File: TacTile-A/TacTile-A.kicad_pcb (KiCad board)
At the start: 2 copper layers, 60 x 60 mm, 100 parts, among them J1 Conn_01x01, J2 Conn_01x01, J3 Conn_01x01, J4 Conn_01x01, U1 MCP14A0304xMNY, U10 MCP14A0304xMNY, U11 MCP14A0304xMNY, U12 MCP14A0304xMNY, U13 MCP14A0304xMNY, U14 MCP14A0304xMNY, U15 MCP14A0304xMNY, U16 MCP14A0304xMNY, U2 MCP14A0304xMNY, U3 MCP14A0304xMNY, U4 MCP14A0304xMNY, U5 MCP14A0304xMNY, U6 MCP14A0304xMNY, U7 MCP14A0304xMNY, U8 MCP14A0304xMNY, U9 MCP14A0304xMNY

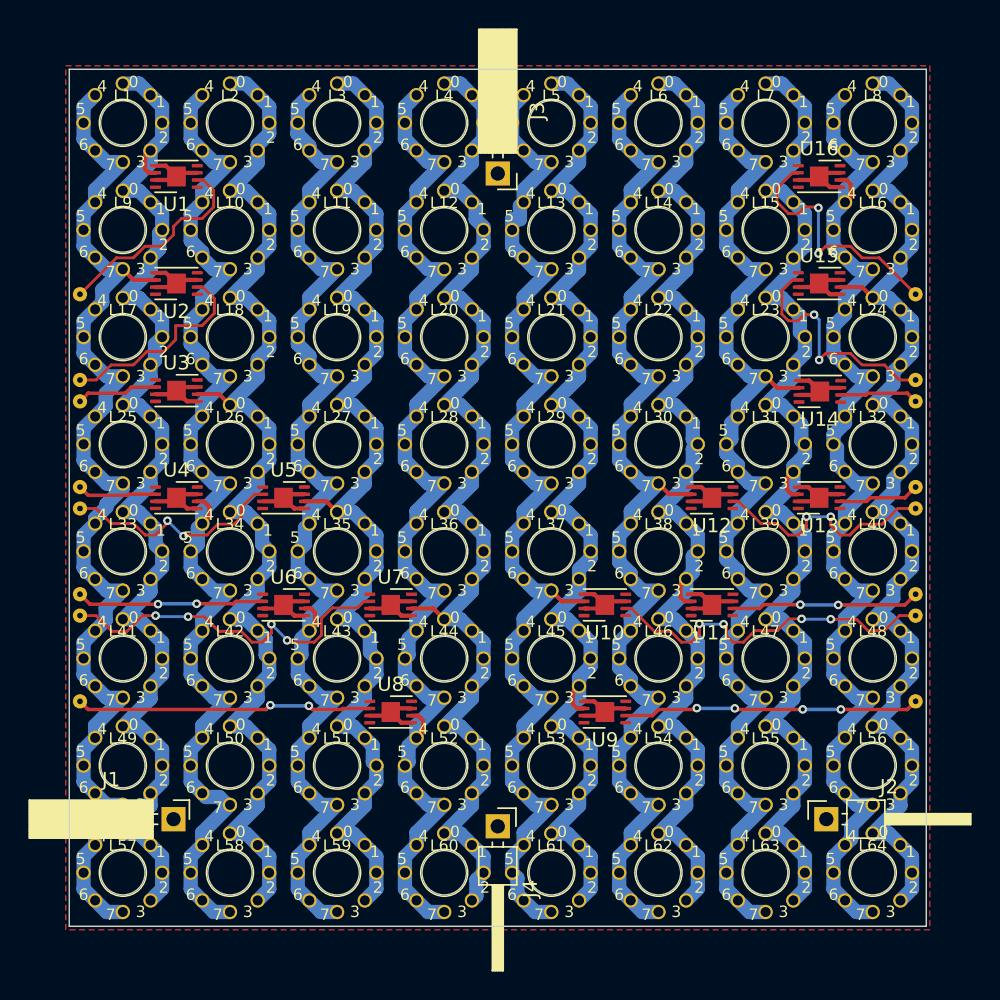
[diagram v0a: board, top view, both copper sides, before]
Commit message: Redid A board with MOSFETs sinking current
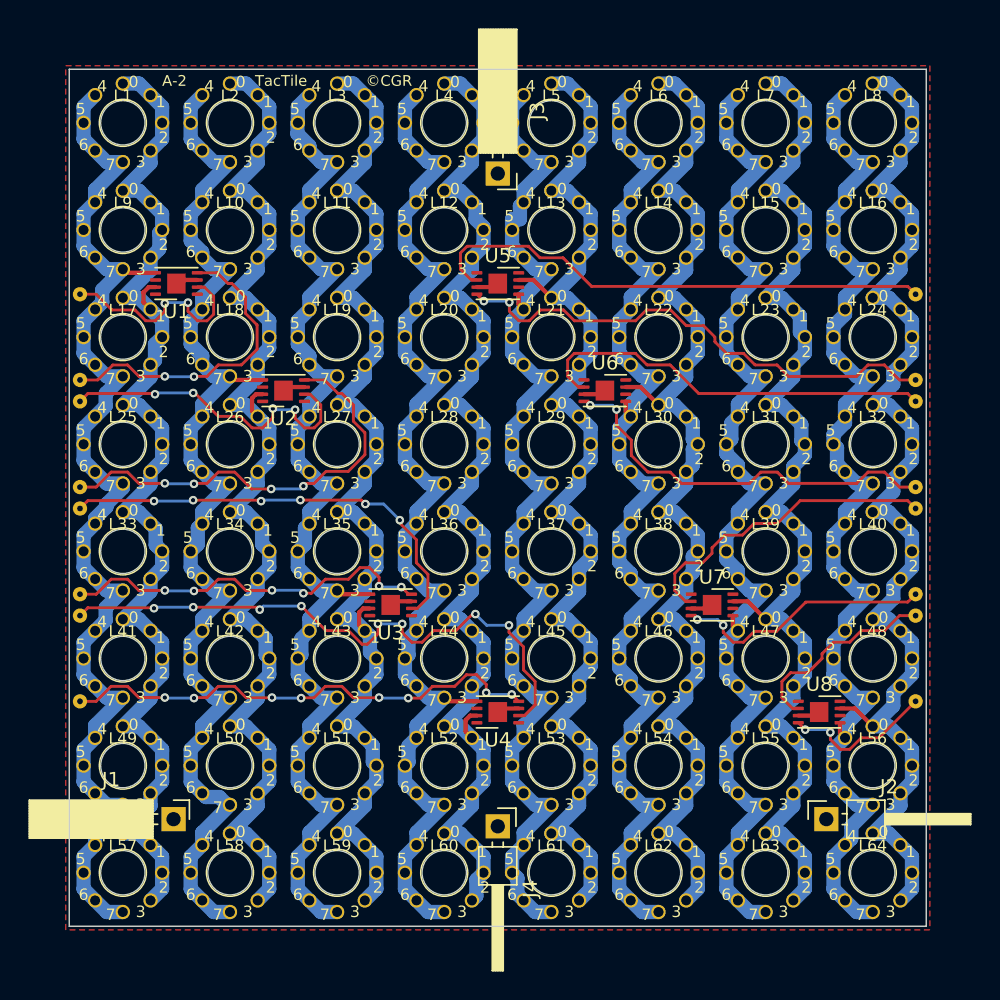
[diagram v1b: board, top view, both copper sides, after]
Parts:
- removed U13, U14, U15, U16: MCP14A0304xMNY, Package_DFN_QFN:WDFN-8-1EP_3x2mm_P0.5mm_EP1.3x1.4mm
- removed the U5 at (40.0, 55.0)
- removed the U6 at (40.0, 62.5)
- removed the U7 at (47.5, 62.5)
- removed the U8 at (47.5, 70.0)
- U1, U2, U3, U4: value MCP14A0304xMNY -> MCP14A0303xMNY
- U5: renamed from U9; value MCP14A0304xMNY -> MCP14A0303xMNY
- U6: renamed from U10; value MCP14A0304xMNY -> MCP14A0303xMNY
- U7: renamed from U11; value MCP14A0304xMNY -> MCP14A0303xMNY
- U8: renamed from U12; value MCP14A0304xMNY -> MCP14A0303xMNY
- moved U5 30.9 mm to (55.0, 40.0), turned to 0 degrees
- moved JMP16 28.5 mm to (84.2, 69.2), turned to 180 degrees
- moved JMP9 28.5 mm to (84.2, 40.8), turned to 180 degrees
- moved U4 27.0 mm to (55.0, 70.0), turned to 180 degrees
- moved U3 21.2 mm to (47.5, 62.5), turned to 180 degrees
- moved U8 16.8 mm to (77.5, 70.0), turned to 0 degrees
- moved JMP10 16.5 mm to (84.2, 46.8), turned to 180 degrees
- moved JMP15 16.5 mm to (84.2, 63.2), turned to 180 degrees
- moved U6 15.0 mm to (62.5, 47.5), turned to 0 degrees
- moved JMP11 13.5 mm to (84.2, 48.2), turned to 180 degrees
- moved JMP14 13.5 mm to (84.2, 61.8), turned to 180 degrees
- moved U2 10.6 mm to (40.0, 47.5)
- moved U1 7.50 mm to (32.5, 40.0)
- moved JMP12 1.50 mm to (84.2, 54.2), turned to 180 degrees
- moved JMP13 1.50 mm to (84.2, 55.8), turned to 180 degrees
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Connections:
- L1 pad 1: /GND1 -> /GND0
- L1 pad 2: /GND1 -> /GND0
- L1 pad 3: /GND1 -> /GND0
- L1 pad 4: /GND1 -> /GND0
- L1 pad 5: /GND2 -> /GND1
- L1 pad 6: /GND2 -> /GND1
- L1 pad 7: /GND2 -> /GND1
- L1 pad 8: /GND2 -> /GND1
- L10 pad 1: /GND3 -> /GND2
- L10 pad 2: /GND3 -> /GND2
- L10 pad 3: /GND3 -> /GND2
- L10 pad 4: /GND3 -> /GND2
- L10 pad 5: /GND4 -> /GND3
- L10 pad 6: /GND4 -> /GND3
- L10 pad 7: /GND4 -> /GND3
- L10 pad 8: /GND4 -> /GND3
- L11 pad 1: /GND5 -> /GND4
- L11 pad 2: /GND5 -> /GND4
- L11 pad 3: /GND5 -> /GND4
- L11 pad 4: /GND5 -> /GND4
- L11 pad 5: /GND6 -> /GND5
- L11 pad 6: /GND6 -> /GND5
- L11 pad 7: /GND6 -> /GND5
- L11 pad 8: /GND6 -> /GND5
- L12 pad 1: /GND7 -> /GND6
- L12 pad 2: /GND7 -> /GND6
- L12 pad 3: /GND7 -> /GND6
- L12 pad 4: /GND7 -> /GND6
- L12 pad 5: /GND8 -> /GND7
- L12 pad 6: /GND8 -> /GND7
- L12 pad 7: /GND8 -> /GND7
- L12 pad 8: /GND8 -> /GND7
- L13 pad 1: /GND9 -> /GND8
- L13 pad 2: /GND9 -> /GND8
- L13 pad 3: /GND9 -> /GND8
- L13 pad 4: /GND9 -> /GND8
- L13 pad 5: /GND10 -> /GND9
- L13 pad 6: /GND10 -> /GND9
- L13 pad 7: /GND10 -> /GND9
- L13 pad 8: /GND10 -> /GND9
- L14 pad 1: /GND11 -> /GND10
- L14 pad 2: /GND11 -> /GND10
- L14 pad 3: /GND11 -> /GND10
- L14 pad 4: /GND11 -> /GND10
- L14 pad 5: /GND12 -> /GND11
- L14 pad 6: /GND12 -> /GND11
- L14 pad 7: /GND12 -> /GND11
- L14 pad 8: /GND12 -> /GND11
- L15 pad 1: /GND13 -> /GND12
- L15 pad 2: /GND13 -> /GND12
- L15 pad 3: /GND13 -> /GND12
- L15 pad 4: /GND13 -> /GND12
- L15 pad 5: /GND14 -> /GND13
- L15 pad 6: /GND14 -> /GND13
- L15 pad 7: /GND14 -> /GND13
- L15 pad 8: /GND14 -> /GND13
- L16 pad 1: /GND15 -> /GND14
- L16 pad 2: /GND15 -> /GND14
- L16 pad 3: /GND15 -> /GND14
- L16 pad 4: /GND15 -> /GND14
- L16 pad 5: /GND16 -> /GND15
- L16 pad 6: /GND16 -> /GND15
- L16 pad 7: /GND16 -> /GND15
- L16 pad 8: /GND16 -> /GND15
- L17 pad 1: /GND1 -> /GND0
- L17 pad 2: /GND1 -> /GND0
- L17 pad 3: /GND1 -> /GND0
- L17 pad 4: /GND1 -> /GND0
- L17 pad 5: /GND2 -> /GND1
- L17 pad 6: /GND2 -> /GND1
- L17 pad 7: /GND2 -> /GND1
- L17 pad 8: /GND2 -> /GND1
- L18 pad 1: /GND3 -> /GND2
- L18 pad 2: /GND3 -> /GND2
- L18 pad 3: /GND3 -> /GND2
- L18 pad 4: /GND3 -> /GND2
- L18 pad 5: /GND4 -> /GND3
- L18 pad 6: /GND4 -> /GND3
- L18 pad 7: /GND4 -> /GND3
- L18 pad 8: /GND4 -> /GND3
- L19 pad 1: /GND5 -> /GND4
- L19 pad 2: /GND5 -> /GND4
- L19 pad 3: /GND5 -> /GND4
- L19 pad 4: /GND5 -> /GND4
- L19 pad 5: /GND6 -> /GND5
- L19 pad 6: /GND6 -> /GND5
- L19 pad 7: /GND6 -> /GND5
- L19 pad 8: /GND6 -> /GND5
- L2 pad 1: /GND3 -> /GND2
- L2 pad 2: /GND3 -> /GND2
- L2 pad 3: /GND3 -> /GND2
- L2 pad 4: /GND3 -> /GND2
- L2 pad 5: /GND4 -> /GND3
- L2 pad 6: /GND4 -> /GND3
- L2 pad 7: /GND4 -> /GND3
- L2 pad 8: /GND4 -> /GND3
- L20 pad 1: /GND7 -> /GND6
- L20 pad 2: /GND7 -> /GND6
- L20 pad 3: /GND7 -> /GND6
- L20 pad 4: /GND7 -> /GND6
- L20 pad 5: /GND8 -> /GND7
- L20 pad 6: /GND8 -> /GND7
- L20 pad 7: /GND8 -> /GND7
- L20 pad 8: /GND8 -> /GND7
- L21 pad 1: /GND9 -> /GND8
- L21 pad 2: /GND9 -> /GND8
- L21 pad 3: /GND9 -> /GND8
- L21 pad 4: /GND9 -> /GND8
- L21 pad 5: /GND10 -> /GND9
- L21 pad 6: /GND10 -> /GND9
- L21 pad 7: /GND10 -> /GND9
- L21 pad 8: /GND10 -> /GND9
- L22 pad 1: /GND11 -> /GND10
- L22 pad 2: /GND11 -> /GND10
- L22 pad 3: /GND11 -> /GND10
- L22 pad 4: /GND11 -> /GND10
- L22 pad 5: /GND12 -> /GND11
- L22 pad 6: /GND12 -> /GND11
- L22 pad 7: /GND12 -> /GND11
- L22 pad 8: /GND12 -> /GND11
- L23 pad 1: /GND13 -> /GND12
- L23 pad 2: /GND13 -> /GND12
- L23 pad 3: /GND13 -> /GND12
- L23 pad 4: /GND13 -> /GND12
- L23 pad 5: /GND14 -> /GND13
- L23 pad 6: /GND14 -> /GND13
- L23 pad 7: /GND14 -> /GND13
- L23 pad 8: /GND14 -> /GND13
- L24 pad 1: /GND15 -> /GND14
- L24 pad 2: /GND15 -> /GND14
- L24 pad 3: /GND15 -> /GND14
- L24 pad 4: /GND15 -> /GND14
- L24 pad 5: /GND16 -> /GND15
- L24 pad 6: /GND16 -> /GND15
- L24 pad 7: /GND16 -> /GND15
- L24 pad 8: /GND16 -> /GND15
- L25 pad 1: /GND1 -> /GND0
- L25 pad 2: /GND1 -> /GND0
- L25 pad 3: /GND1 -> /GND0
- L25 pad 4: /GND1 -> /GND0
- L25 pad 5: /GND2 -> /GND1
- L25 pad 6: /GND2 -> /GND1
- L25 pad 7: /GND2 -> /GND1
- L25 pad 8: /GND2 -> /GND1
- L26 pad 1: /GND3 -> /GND2
- L26 pad 2: /GND3 -> /GND2
- L26 pad 3: /GND3 -> /GND2
- L26 pad 4: /GND3 -> /GND2
- L26 pad 5: /GND4 -> /GND3
- L26 pad 6: /GND4 -> /GND3
- L26 pad 7: /GND4 -> /GND3
- L26 pad 8: /GND4 -> /GND3
- L27 pad 1: /GND5 -> /GND4
- L27 pad 2: /GND5 -> /GND4
- L27 pad 3: /GND5 -> /GND4
- L27 pad 4: /GND5 -> /GND4
- L27 pad 5: /GND6 -> /GND5
- L27 pad 6: /GND6 -> /GND5
- L27 pad 7: /GND6 -> /GND5
- L27 pad 8: /GND6 -> /GND5
- L28 pad 1: /GND7 -> /GND6
- L28 pad 2: /GND7 -> /GND6
- L28 pad 3: /GND7 -> /GND6
- L28 pad 4: /GND7 -> /GND6
- L28 pad 5: /GND8 -> /GND7
- L28 pad 6: /GND8 -> /GND7
- L28 pad 7: /GND8 -> /GND7
- L28 pad 8: /GND8 -> /GND7
- L29 pad 1: /GND9 -> /GND8
- L29 pad 2: /GND9 -> /GND8
- L29 pad 3: /GND9 -> /GND8
- L29 pad 4: /GND9 -> /GND8
- L29 pad 5: /GND10 -> /GND9
- L29 pad 6: /GND10 -> /GND9
- L29 pad 7: /GND10 -> /GND9
- L29 pad 8: /GND10 -> /GND9
- L3 pad 1: /GND5 -> /GND4
- L3 pad 2: /GND5 -> /GND4
- L3 pad 3: /GND5 -> /GND4
- L3 pad 4: /GND5 -> /GND4
- L3 pad 5: /GND6 -> /GND5
- L3 pad 6: /GND6 -> /GND5
- L3 pad 7: /GND6 -> /GND5
- L3 pad 8: /GND6 -> /GND5
- L30 pad 1: /GND11 -> /GND10
- L30 pad 2: /GND11 -> /GND10
- L30 pad 3: /GND11 -> /GND10
- L30 pad 4: /GND11 -> /GND10
- L30 pad 5: /GND12 -> /GND11
- L30 pad 6: /GND12 -> /GND11
- L30 pad 7: /GND12 -> /GND11
- L30 pad 8: /GND12 -> /GND11
- L31 pad 1: /GND13 -> /GND12
- L31 pad 2: /GND13 -> /GND12
- L31 pad 3: /GND13 -> /GND12
- L31 pad 4: /GND13 -> /GND12
- L31 pad 5: /GND14 -> /GND13
- L31 pad 6: /GND14 -> /GND13
- L31 pad 7: /GND14 -> /GND13
- L31 pad 8: /GND14 -> /GND13
- L32 pad 1: /GND15 -> /GND14
- L32 pad 2: /GND15 -> /GND14
- L32 pad 3: /GND15 -> /GND14
- L32 pad 4: /GND15 -> /GND14
- L32 pad 5: /GND16 -> /GND15
- L32 pad 6: /GND16 -> /GND15
- L32 pad 7: /GND16 -> /GND15
- L32 pad 8: /GND16 -> /GND15
- L33 pad 1: /GND1 -> /GND0
- L33 pad 2: /GND1 -> /GND0
- L33 pad 3: /GND1 -> /GND0
- L33 pad 4: /GND1 -> /GND0
- L33 pad 5: /GND2 -> /GND1
- L33 pad 6: /GND2 -> /GND1
- L33 pad 7: /GND2 -> /GND1
- L33 pad 8: /GND2 -> /GND1
- L34 pad 1: /GND3 -> /GND2
- L34 pad 2: /GND3 -> /GND2
- L34 pad 3: /GND3 -> /GND2
- L34 pad 4: /GND3 -> /GND2
- L34 pad 5: /GND4 -> /GND3
- L34 pad 6: /GND4 -> /GND3
- L34 pad 7: /GND4 -> /GND3
- L34 pad 8: /GND4 -> /GND3
- L35 pad 1: /GND5 -> /GND4
- L35 pad 2: /GND5 -> /GND4
- L35 pad 3: /GND5 -> /GND4
- L35 pad 4: /GND5 -> /GND4
- L35 pad 5: /GND6 -> /GND5
- L35 pad 6: /GND6 -> /GND5
- L35 pad 7: /GND6 -> /GND5
- L35 pad 8: /GND6 -> /GND5
- L36 pad 1: /GND7 -> /GND6
- L36 pad 2: /GND7 -> /GND6
- L36 pad 3: /GND7 -> /GND6
- L36 pad 4: /GND7 -> /GND6
- L36 pad 5: /GND8 -> /GND7
- L36 pad 6: /GND8 -> /GND7
- L36 pad 7: /GND8 -> /GND7
- L36 pad 8: /GND8 -> /GND7
- L37 pad 1: /GND9 -> /GND8
- L37 pad 2: /GND9 -> /GND8
- L37 pad 3: /GND9 -> /GND8
- L37 pad 4: /GND9 -> /GND8
- L37 pad 5: /GND10 -> /GND9
- L37 pad 6: /GND10 -> /GND9
- L37 pad 7: /GND10 -> /GND9
- L37 pad 8: /GND10 -> /GND9
- L38 pad 1: /GND11 -> /GND10
- L38 pad 2: /GND11 -> /GND10
- L38 pad 3: /GND11 -> /GND10
- L38 pad 4: /GND11 -> /GND10
- L38 pad 5: /GND12 -> /GND11
- L38 pad 6: /GND12 -> /GND11
- L38 pad 7: /GND12 -> /GND11
- L38 pad 8: /GND12 -> /GND11
- L39 pad 1: /GND13 -> /GND12
- L39 pad 2: /GND13 -> /GND12
- L39 pad 3: /GND13 -> /GND12
- L39 pad 4: /GND13 -> /GND12
- L39 pad 5: /GND14 -> /GND13
- L39 pad 6: /GND14 -> /GND13
- L39 pad 7: /GND14 -> /GND13
- L39 pad 8: /GND14 -> /GND13
- L4 pad 1: /GND7 -> /GND6
- L4 pad 2: /GND7 -> /GND6
- L4 pad 3: /GND7 -> /GND6
- L4 pad 4: /GND7 -> /GND6
- L4 pad 5: /GND8 -> /GND7
- L4 pad 6: /GND8 -> /GND7
- L4 pad 7: /GND8 -> /GND7
- L4 pad 8: /GND8 -> /GND7
- L40 pad 1: /GND15 -> /GND14
- L40 pad 2: /GND15 -> /GND14
- L40 pad 3: /GND15 -> /GND14
- L40 pad 4: /GND15 -> /GND14
- L40 pad 5: /GND16 -> /GND15
- L40 pad 6: /GND16 -> /GND15
- L40 pad 7: /GND16 -> /GND15
- L40 pad 8: /GND16 -> /GND15
- L41 pad 1: /GND1 -> /GND0
- L41 pad 2: /GND1 -> /GND0
- L41 pad 3: /GND1 -> /GND0
- L41 pad 4: /GND1 -> /GND0
- L41 pad 5: /GND2 -> /GND1
- L41 pad 6: /GND2 -> /GND1
- L41 pad 7: /GND2 -> /GND1
- L41 pad 8: /GND2 -> /GND1
- L42 pad 1: /GND3 -> /GND2
- L42 pad 2: /GND3 -> /GND2
- L42 pad 3: /GND3 -> /GND2
- L42 pad 4: /GND3 -> /GND2
- L42 pad 5: /GND4 -> /GND3
- L42 pad 6: /GND4 -> /GND3
- L42 pad 7: /GND4 -> /GND3
- L42 pad 8: /GND4 -> /GND3
- L43 pad 1: /GND5 -> /GND4
- L43 pad 2: /GND5 -> /GND4
- L43 pad 3: /GND5 -> /GND4
- L43 pad 4: /GND5 -> /GND4
- L43 pad 5: /GND6 -> /GND5
- L43 pad 6: /GND6 -> /GND5
- L43 pad 7: /GND6 -> /GND5
- L43 pad 8: /GND6 -> /GND5
- L44 pad 1: /GND7 -> /GND6
- L44 pad 2: /GND7 -> /GND6
- L44 pad 3: /GND7 -> /GND6
- L44 pad 4: /GND7 -> /GND6
- L44 pad 5: /GND8 -> /GND7
- L44 pad 6: /GND8 -> /GND7
- L44 pad 7: /GND8 -> /GND7
- L44 pad 8: /GND8 -> /GND7
- L45 pad 1: /GND9 -> /GND8
- L45 pad 2: /GND9 -> /GND8
- L45 pad 3: /GND9 -> /GND8
- L45 pad 4: /GND9 -> /GND8
- L45 pad 5: /GND10 -> /GND9
- L45 pad 6: /GND10 -> /GND9
- L45 pad 7: /GND10 -> /GND9
- L45 pad 8: /GND10 -> /GND9
- L46 pad 1: /GND11 -> /GND10
- L46 pad 2: /GND11 -> /GND10
- L46 pad 3: /GND11 -> /GND10
- L46 pad 4: /GND11 -> /GND10
- L46 pad 5: /GND12 -> /GND11
- L46 pad 6: /GND12 -> /GND11
- L46 pad 7: /GND12 -> /GND11
- L46 pad 8: /GND12 -> /GND11
- L47 pad 1: /GND13 -> /GND12
- L47 pad 2: /GND13 -> /GND12
- L47 pad 3: /GND13 -> /GND12
- L47 pad 4: /GND13 -> /GND12
- L47 pad 5: /GND14 -> /GND13
- L47 pad 6: /GND14 -> /GND13
- L47 pad 7: /GND14 -> /GND13
- L47 pad 8: /GND14 -> /GND13
- L48 pad 1: /GND15 -> /GND14
- L48 pad 2: /GND15 -> /GND14
- L48 pad 3: /GND15 -> /GND14
- L48 pad 4: /GND15 -> /GND14
- L48 pad 5: /GND16 -> /GND15
- L48 pad 6: /GND16 -> /GND15
- L48 pad 7: /GND16 -> /GND15
- L48 pad 8: /GND16 -> /GND15
- L49 pad 1: /GND1 -> /GND0
- L49 pad 2: /GND1 -> /GND0
- L49 pad 3: /GND1 -> /GND0
- L49 pad 4: /GND1 -> /GND0
- L49 pad 5: /GND2 -> /GND1
- L49 pad 6: /GND2 -> /GND1
- L49 pad 7: /GND2 -> /GND1
- L49 pad 8: /GND2 -> /GND1
- L5 pad 1: /GND9 -> /GND8
- L5 pad 2: /GND9 -> /GND8
- L5 pad 3: /GND9 -> /GND8
- L5 pad 4: /GND9 -> /GND8
- L5 pad 5: /GND10 -> /GND9
- L5 pad 6: /GND10 -> /GND9
- L5 pad 7: /GND10 -> /GND9
- L5 pad 8: /GND10 -> /GND9
- L50 pad 1: /GND3 -> /GND2
- L50 pad 2: /GND3 -> /GND2
- L50 pad 3: /GND3 -> /GND2
- L50 pad 4: /GND3 -> /GND2
- L50 pad 5: /GND4 -> /GND3
- L50 pad 6: /GND4 -> /GND3
- L50 pad 7: /GND4 -> /GND3
- L50 pad 8: /GND4 -> /GND3
- L51 pad 1: /GND5 -> /GND4
- L51 pad 2: /GND5 -> /GND4
- L51 pad 3: /GND5 -> /GND4
- L51 pad 4: /GND5 -> /GND4
- L51 pad 5: /GND6 -> /GND5
- L51 pad 6: /GND6 -> /GND5
- L51 pad 7: /GND6 -> /GND5
- L51 pad 8: /GND6 -> /GND5
- L52 pad 1: /GND7 -> /GND6
- L52 pad 2: /GND7 -> /GND6
- L52 pad 3: /GND7 -> /GND6
- L52 pad 4: /GND7 -> /GND6
- L52 pad 5: /GND8 -> /GND7
- L52 pad 6: /GND8 -> /GND7
- L52 pad 7: /GND8 -> /GND7
- L52 pad 8: /GND8 -> /GND7
- L53 pad 1: /GND9 -> /GND8
- L53 pad 2: /GND9 -> /GND8
- L53 pad 3: /GND9 -> /GND8
- L53 pad 4: /GND9 -> /GND8
- L53 pad 5: /GND10 -> /GND9
- L53 pad 6: /GND10 -> /GND9
- L53 pad 7: /GND10 -> /GND9
- L53 pad 8: /GND10 -> /GND9
- L54 pad 1: /GND11 -> /GND10
- L54 pad 2: /GND11 -> /GND10
- L54 pad 3: /GND11 -> /GND10
- L54 pad 4: /GND11 -> /GND10
- L54 pad 5: /GND12 -> /GND11
- L54 pad 6: /GND12 -> /GND11
- L54 pad 7: /GND12 -> /GND11
- L54 pad 8: /GND12 -> /GND11
- L55 pad 1: /GND13 -> /GND12
- L55 pad 2: /GND13 -> /GND12
- L55 pad 3: /GND13 -> /GND12
- L55 pad 4: /GND13 -> /GND12
- L55 pad 5: /GND14 -> /GND13
- L55 pad 6: /GND14 -> /GND13
- L55 pad 7: /GND14 -> /GND13
- L55 pad 8: /GND14 -> /GND13
- L56 pad 1: /GND15 -> /GND14
- L56 pad 2: /GND15 -> /GND14
- L56 pad 3: /GND15 -> /GND14
- L56 pad 4: /GND15 -> /GND14
- L56 pad 5: /GND16 -> /GND15
- L56 pad 6: /GND16 -> /GND15
- L56 pad 7: /GND16 -> /GND15
- L56 pad 8: /GND16 -> /GND15
- L57 pad 1: /GND1 -> /GND0
- L57 pad 2: /GND1 -> /GND0
- L57 pad 3: /GND1 -> /GND0
- L57 pad 4: /GND1 -> /GND0
- L57 pad 5: /GND2 -> /GND1
- L57 pad 6: /GND2 -> /GND1
- L57 pad 7: /GND2 -> /GND1
- L57 pad 8: /GND2 -> /GND1
- L58 pad 1: /GND3 -> /GND2
- L58 pad 2: /GND3 -> /GND2
- L58 pad 3: /GND3 -> /GND2
- L58 pad 4: /GND3 -> /GND2
- L58 pad 5: /GND4 -> /GND3
- L58 pad 6: /GND4 -> /GND3
- L58 pad 7: /GND4 -> /GND3
- L58 pad 8: /GND4 -> /GND3
- L59 pad 1: /GND5 -> /GND4
- L59 pad 2: /GND5 -> /GND4
- L59 pad 3: /GND5 -> /GND4
- L59 pad 4: /GND5 -> /GND4
- L59 pad 5: /GND6 -> /GND5
- L59 pad 6: /GND6 -> /GND5
- L59 pad 7: /GND6 -> /GND5
- L59 pad 8: /GND6 -> /GND5
- L6 pad 1: /GND11 -> /GND10
- L6 pad 2: /GND11 -> /GND10
- L6 pad 3: /GND11 -> /GND10
- L6 pad 4: /GND11 -> /GND10
- L6 pad 5: /GND12 -> /GND11
- L6 pad 6: /GND12 -> /GND11
- L6 pad 7: /GND12 -> /GND11
- L6 pad 8: /GND12 -> /GND11
- L60 pad 1: /GND7 -> /GND6
- L60 pad 2: /GND7 -> /GND6
- L60 pad 3: /GND7 -> /GND6
- L60 pad 4: /GND7 -> /GND6
- L60 pad 5: /GND8 -> /GND7
- L60 pad 6: /GND8 -> /GND7
- L60 pad 7: /GND8 -> /GND7
- L60 pad 8: /GND8 -> /GND7
- L61 pad 1: /GND9 -> /GND8
- L61 pad 2: /GND9 -> /GND8
- L61 pad 3: /GND9 -> /GND8
- L61 pad 4: /GND9 -> /GND8
- L61 pad 5: /GND10 -> /GND9
- L61 pad 6: /GND10 -> /GND9
- L61 pad 7: /GND10 -> /GND9
- L61 pad 8: /GND10 -> /GND9
- L62 pad 1: /GND11 -> /GND10
- L62 pad 2: /GND11 -> /GND10
- L62 pad 3: /GND11 -> /GND10
- L62 pad 4: /GND11 -> /GND10
- L62 pad 5: /GND12 -> /GND11
- L62 pad 6: /GND12 -> /GND11
- L62 pad 7: /GND12 -> /GND11
- L62 pad 8: /GND12 -> /GND11
- L63 pad 1: /GND13 -> /GND12
- L63 pad 2: /GND13 -> /GND12
- L63 pad 3: /GND13 -> /GND12
- L63 pad 4: /GND13 -> /GND12
- L63 pad 5: /GND14 -> /GND13
- L63 pad 6: /GND14 -> /GND13
- L63 pad 7: /GND14 -> /GND13
- L63 pad 8: /GND14 -> /GND13
- L64 pad 1: /GND15 -> /GND14
- L64 pad 2: /GND15 -> /GND14
- L64 pad 3: /GND15 -> /GND14
- L64 pad 4: /GND15 -> /GND14
- L64 pad 5: /GND16 -> /GND15
- L64 pad 6: /GND16 -> /GND15
- L64 pad 7: /GND16 -> /GND15
- L64 pad 8: /GND16 -> /GND15
- L7 pad 1: /GND13 -> /GND12
- L7 pad 2: /GND13 -> /GND12
- L7 pad 3: /GND13 -> /GND12
- L7 pad 4: /GND13 -> /GND12
- L7 pad 5: /GND14 -> /GND13
- L7 pad 6: /GND14 -> /GND13
- L7 pad 7: /GND14 -> /GND13
- L7 pad 8: /GND14 -> /GND13
- L8 pad 1: /GND15 -> /GND14
- L8 pad 2: /GND15 -> /GND14
- L8 pad 3: /GND15 -> /GND14
- L8 pad 4: /GND15 -> /GND14
- L8 pad 5: /GND16 -> /GND15
- L8 pad 6: /GND16 -> /GND15
- L8 pad 7: /GND16 -> /GND15
- L8 pad 8: /GND16 -> /GND15
- L9 pad 1: /GND1 -> /GND0
- L9 pad 2: /GND1 -> /GND0
- L9 pad 3: /GND1 -> /GND0
- L9 pad 4: /GND1 -> /GND0
- L9 pad 5: /GND2 -> /GND1
- L9 pad 6: /GND2 -> /GND1
- L9 pad 7: /GND2 -> /GND1
- L9 pad 8: /GND2 -> /GND1
- U1 pad 4: unconnected-(U1-INB-Pad4) -> /INP1
- U1 pad 5: /GND -> /GND1
- U1 pad 6: /GND1 -> unconnected-(U1-V+-Pad6)
- U1 pad 7: /GND -> /GND0
- U2 pad 2: /INP1 -> /INP2
- U2 pad 4: unconnected-(U2-INB-Pad4) -> /INP3
- U2 pad 5: /GND -> /GND3
- U2 pad 6: /GND2 -> unconnected-(U2-V+-Pad6)
- U2 pad 7: /GND -> /GND2
- U3 pad 2: /INP2 -> /INP4
- U3 pad 4: unconnected-(U3-INB-Pad4) -> /INP5
- U3 pad 5: /GND -> /GND5
- U3 pad 6: /GND3 -> unconnected-(U3-V+-Pad6)
- U3 pad 7: /GND -> /GND4
- U4 pad 2: /INP3 -> /INP6
- U4 pad 4: unconnected-(U4-INB-Pad4) -> /INP7
- U4 pad 5: /GND -> /GND7
- U4 pad 6: /GND4 -> unconnected-(U4-V+-Pad6)
- U4 pad 7: /GND -> /GND6
- U5 pad 4: unconnected-(U9-INB-Pad4) -> /INP9
- U5 pad 5: /GND -> /GND9
- U5 pad 6: /GND9 -> unconnected-(U5-V+-Pad6)
- U5 pad 7: /GND -> /GND8
- U6 pad 2: /INP9 -> /INP10
- U6 pad 4: unconnected-(U10-INB-Pad4) -> /INP11
- U6 pad 5: /GND -> /GND11
- U6 pad 6: /GND10 -> unconnected-(U6-V+-Pad6)
- U6 pad 7: /GND -> /GND10
- U7 pad 2: /INP10 -> /INP12
- U7 pad 4: unconnected-(U11-INB-Pad4) -> /INP13
- U7 pad 5: /GND -> /GND13
- U7 pad 6: /GND11 -> unconnected-(U7-V+-Pad6)
- U7 pad 7: /GND -> /GND12
- U8 pad 2: /INP11 -> /INP14
- U8 pad 4: unconnected-(U12-INB-Pad4) -> /INP15
- U8 pad 5: /GND -> /GND15
- U8 pad 6: /GND12 -> unconnected-(U8-V+-Pad6)
- U8 pad 7: /GND -> /GND14
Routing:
- net /GND0: track 0.00 -> 82.3 mm
- net /GND16: track 82.2 -> 0.00 mm
- net /GND: track 78.5 -> 12.5 mm
- net /INP3: track 5.56 -> 30.5 mm, vias 0 -> 4
- net /INP6: track 25.2 -> 42.5 mm, vias 4 -> 8
- net /INP2: track 5.70 -> 22.8 mm, vias 0 -> 4
- net /INP12: track 5.70 -> 22.1 mm
- net /INP10: track 13.2 -> 28.5 mm, vias 2 -> 0
- net /INP8: track 20.8 -> 36.0 mm, vias 4 -> 0
- net /INP4: track 16.1 -> 31.1 mm, vias 2 -> 6
- net /INP7: track 20.8 -> 34.7 mm, vias 2 -> 8
- net /INP5: track 13.2 -> 26.6 mm, vias 2 -> 6
- net /INP13: track 5.53 -> 18.2 mm, vias 0 -> 2
- net /INP11: track 16.4 -> 28.3 mm
- net /INP9: track 24.5 -> 35.7 mm, vias 4 -> 2
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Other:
- board text added: "A-2"
- board text added: "TacTile"
- board text added: "©CGR"

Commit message: Added voltage input to A MOSFETs
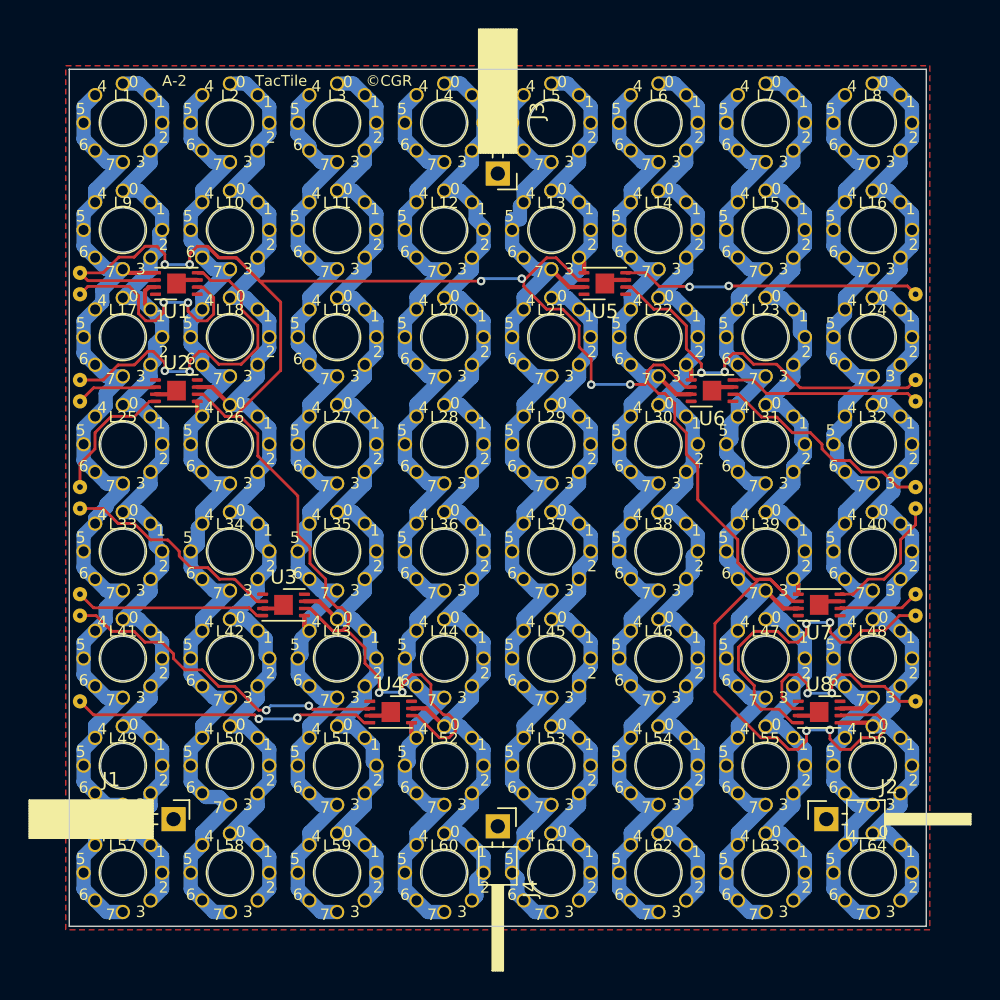
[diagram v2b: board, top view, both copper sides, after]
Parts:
- added JMP17: ~, TacTile:Jumper_Connect, F.Cu at (25.8, 39.2)
- moved U2 7.50 mm to (32.5, 47.5), turned to 0 degrees
- moved U3 7.50 mm to (40.0, 62.5), turned to 0 degrees
- moved U4 7.50 mm to (47.5, 70.0), turned to 0 degrees
- moved U5 7.50 mm to (62.5, 40.0), turned to 180 degrees
- moved U6 7.50 mm to (70.0, 47.5), turned to 180 degrees
- moved U7 7.50 mm to (77.5, 62.5), turned to 180 degrees
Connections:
- U1 pad 6: unconnected-(U1-V+-Pad6) -> /VCC
- U2 pad 6: unconnected-(U2-V+-Pad6) -> /VCC
- U3 pad 6: unconnected-(U3-V+-Pad6) -> /VCC
- U4 pad 6: unconnected-(U4-V+-Pad6) -> /VCC
- U5 pad 2: /INP8 -> /INP9
- U5 pad 4: /INP9 -> /INP8
- U5 pad 5: /GND9 -> /GND8
- U5 pad 6: unconnected-(U5-V+-Pad6) -> /VCC
- U5 pad 7: /GND8 -> /GND9
- U6 pad 2: /INP10 -> /INP11
- U6 pad 4: /INP11 -> /INP10
- U6 pad 5: /GND11 -> /GND10
- U6 pad 6: unconnected-(U6-V+-Pad6) -> /VCC
- U6 pad 7: /GND10 -> /GND11
- U7 pad 2: /INP12 -> /INP13
- U7 pad 4: /INP13 -> /INP12
- U7 pad 5: /GND13 -> /GND12
- U7 pad 6: unconnected-(U7-V+-Pad6) -> /VCC
- U7 pad 7: /GND12 -> /GND13
- U8 pad 2: /INP14 -> /INP15
- U8 pad 4: /INP15 -> /INP14
- U8 pad 5: /GND15 -> /GND14
- U8 pad 6: unconnected-(U8-V+-Pad6) -> /VCC
- U8 pad 7: /GND14 -> /GND15
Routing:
- net /VCC: track 0.00 -> 181.8 mm, vias 0 -> 10
- net /INP3: track 30.5 -> 9.38 mm, vias 4 -> 0
- net /INP6: track 42.5 -> 23.5 mm, vias 8 -> 2
- net /INP2: track 22.8 -> 5.70 mm, vias 4 -> 0
- net /INP4: track 31.1 -> 15.7 mm, vias 6 -> 0
- net /INP10: track 28.5 -> 13.4 mm
- net /INP8: track 36.0 -> 21.0 mm, vias 0 -> 2
- net /INP7: track 34.7 -> 21.1 mm, vias 8 -> 2
- net /INP5: track 26.6 -> 13.4 mm, vias 6 -> 0
- net /INP12: track 22.1 -> 9.38 mm
- net /INP11: track 28.3 -> 15.7 mm, vias 2 -> 0
- net /INP13: track 18.2 -> 5.70 mm, vias 2 -> 0
- net /INP14: track 14.1 -> 23.9 mm, vias 0 -> 2
- net /INP9: track 35.7 -> 26.3 mm
- net /INP15: track 10.7 -> 14.8 mm
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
